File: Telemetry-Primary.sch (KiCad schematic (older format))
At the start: 39 parts, among them J1 CAN_LogicAnalyzer, J2 IMU_LogicAnalyzer, J3 GPS_LogicAnalyzer, J4 RTCC_LogicAnalyzer, J5 SDCard_LogicAnalyzer, J6 SWD, SW1 Reset, U1 STM32F429ZITx, Y1 8M

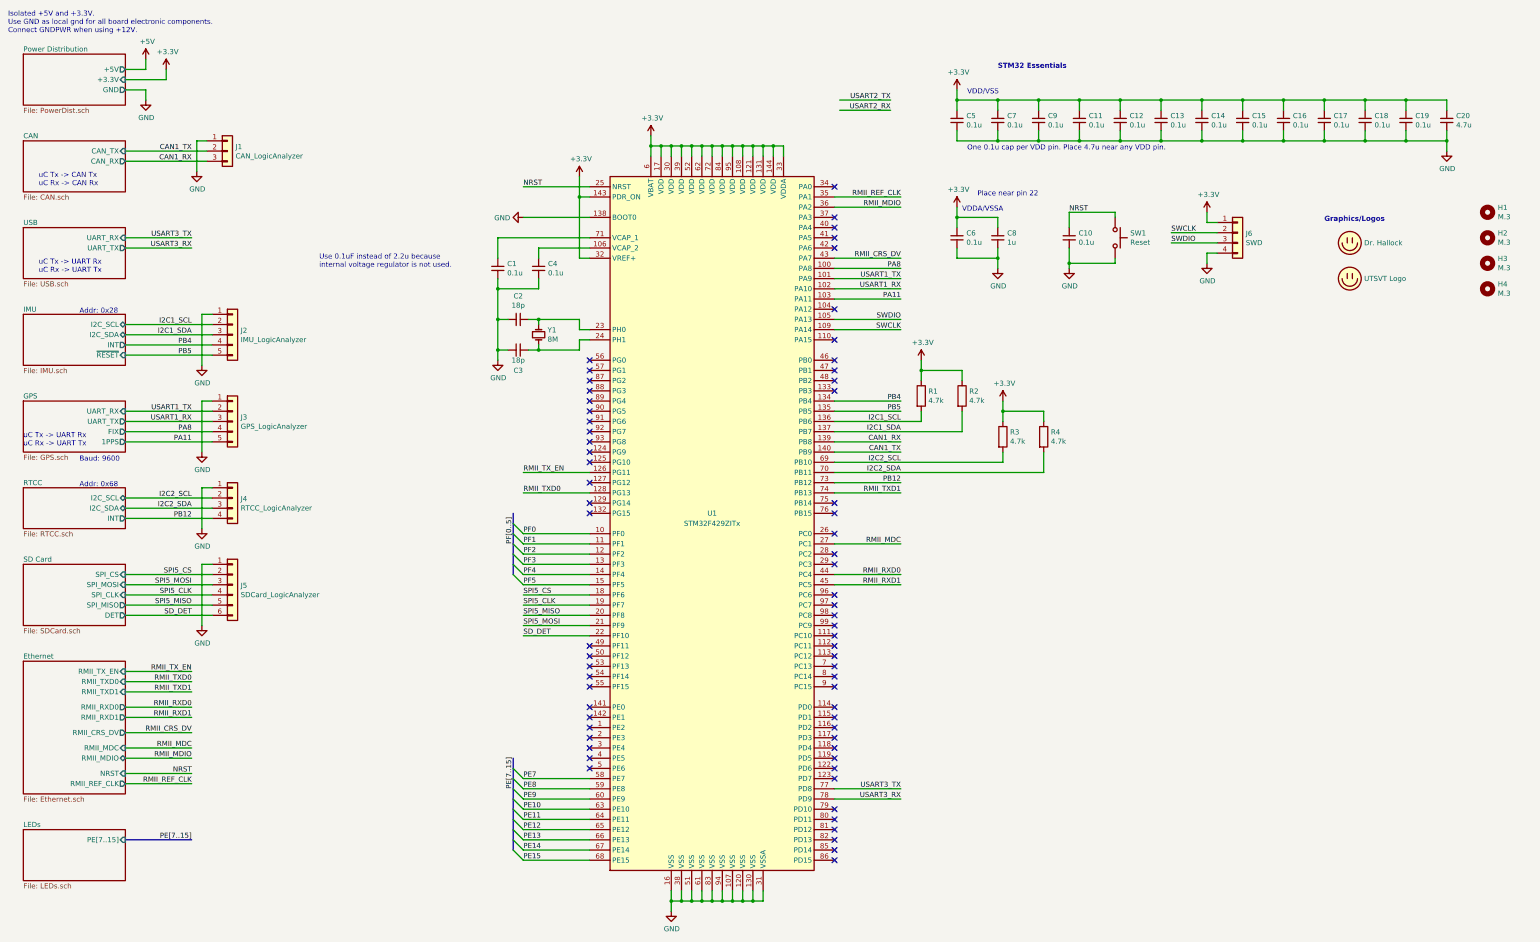
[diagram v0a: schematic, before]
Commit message: Remove the external RTC.
There's no need to use an external RTC on the telemetry board. The
microcontroller itself has an internal RTC that can be powered from
the VBAT line and a 32.768kHz oscillator.
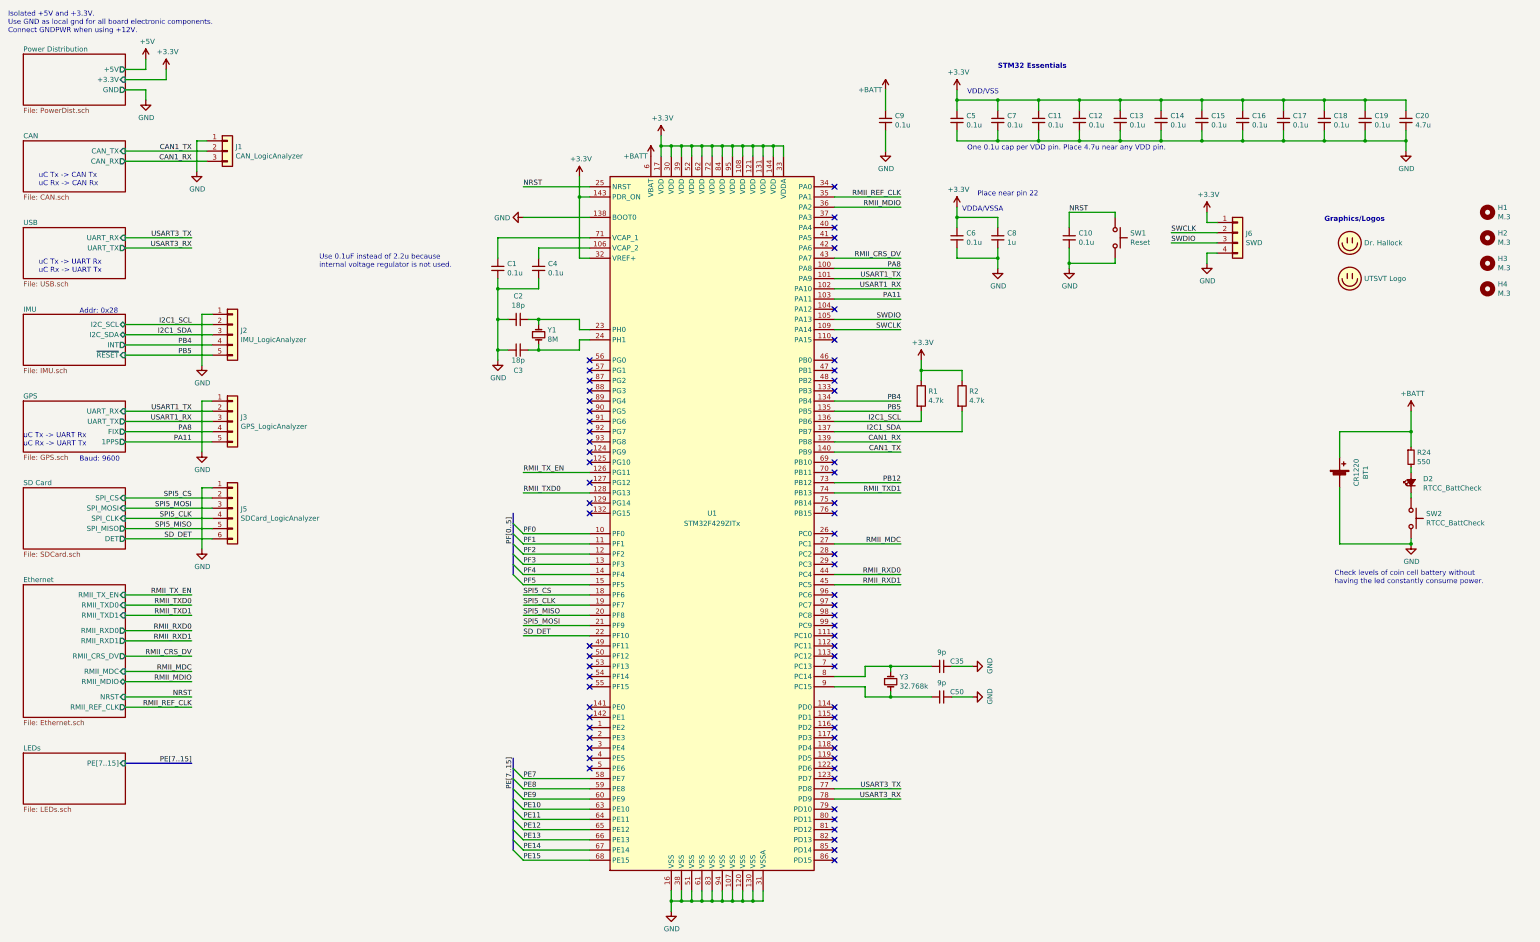
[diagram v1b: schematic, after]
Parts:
- removed J4: RTCC_LogicAnalyzer, Connector_PinHeader_2.54mm:PinHeader_1x04_P2.54mm_Vertical, symbol Connector_Generic:Conn_01x04
- removed R3, R4: 4.7k, Resistor_SMD:R_0805_2012Metric, symbol Device:R
- added BT1: CR1220, Battery:BatteryHolder_Keystone_3000_1x12mm, symbol Device:Battery_Cell
- added C35, C50: 9p, Capacitor_SMD:C_0805_2012Metric, symbol Device:C_Small
- added D2: RTCC_BattCheck, LED_SMD:LED_0805_2012Metric, symbol Device:LED_Small_ALT
- added R24: 550, Resistor_SMD:R_0805_2012Metric, symbol Device:R_Small
- added SW2: RTCC_BattCheck, Button_Switch_SMD:SW_SPST_B3SL-1002P, symbol Switch:SW_Push
- added Y3: 32.768k, Crystal:Crystal_SMD_2012-2Pin_2.0x1.2mm, symbol Device:Crystal_Small
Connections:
- net +3V3: no longer C9.1, U1.6 (VBAT)
- net GND: now also BT1.2 (-), C35.1, C50.1, SW2.2
- net at U1.8 (PC14): now also C35.2, Y3.1
- net at U1.9 (PC15): now also C50.2, Y3.2
- net I2C2_SCL: no longer names the net of U1.69 (PB10)
- net I2C2_SDA: no longer names the net of U1.70 (PB11)
- new net: D2.1 (K), SW2.1
- new net: D2.2 (A), R24.2
- new net +BATT: BT1.1 (+), C9.1, R24.1, U1.6 (VBAT)
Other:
- note added: "Check levels of coin cell battery without\nhaving the led constantly consume power."
- note removed: "Addr: 0x68"
- moved on the sheet: C11, C12, C13, C14, C15, C16, C17, C18, C19, C20, C9, J5
